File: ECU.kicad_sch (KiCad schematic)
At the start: 62 parts, among them J1 Solenoid 0, J10 Thermocouple 3, J2 Solenoid 1, J3 Solenoid 2, J4 Solenoid 3, J5 Solenoid 4, J6 Solenoid 5, J7 Thermocouple 0, J8 Thermocouple 1, J9 Thermocouple 2, U1 Teensy4.1, U10 MAX31855, U11 MAX31855, U2 OPA357, U3 OPA357, U4 OPA357, U5 OPA357, U6 OPA357, U7 OPA357, U8 MAX31855, U9 MAX31855

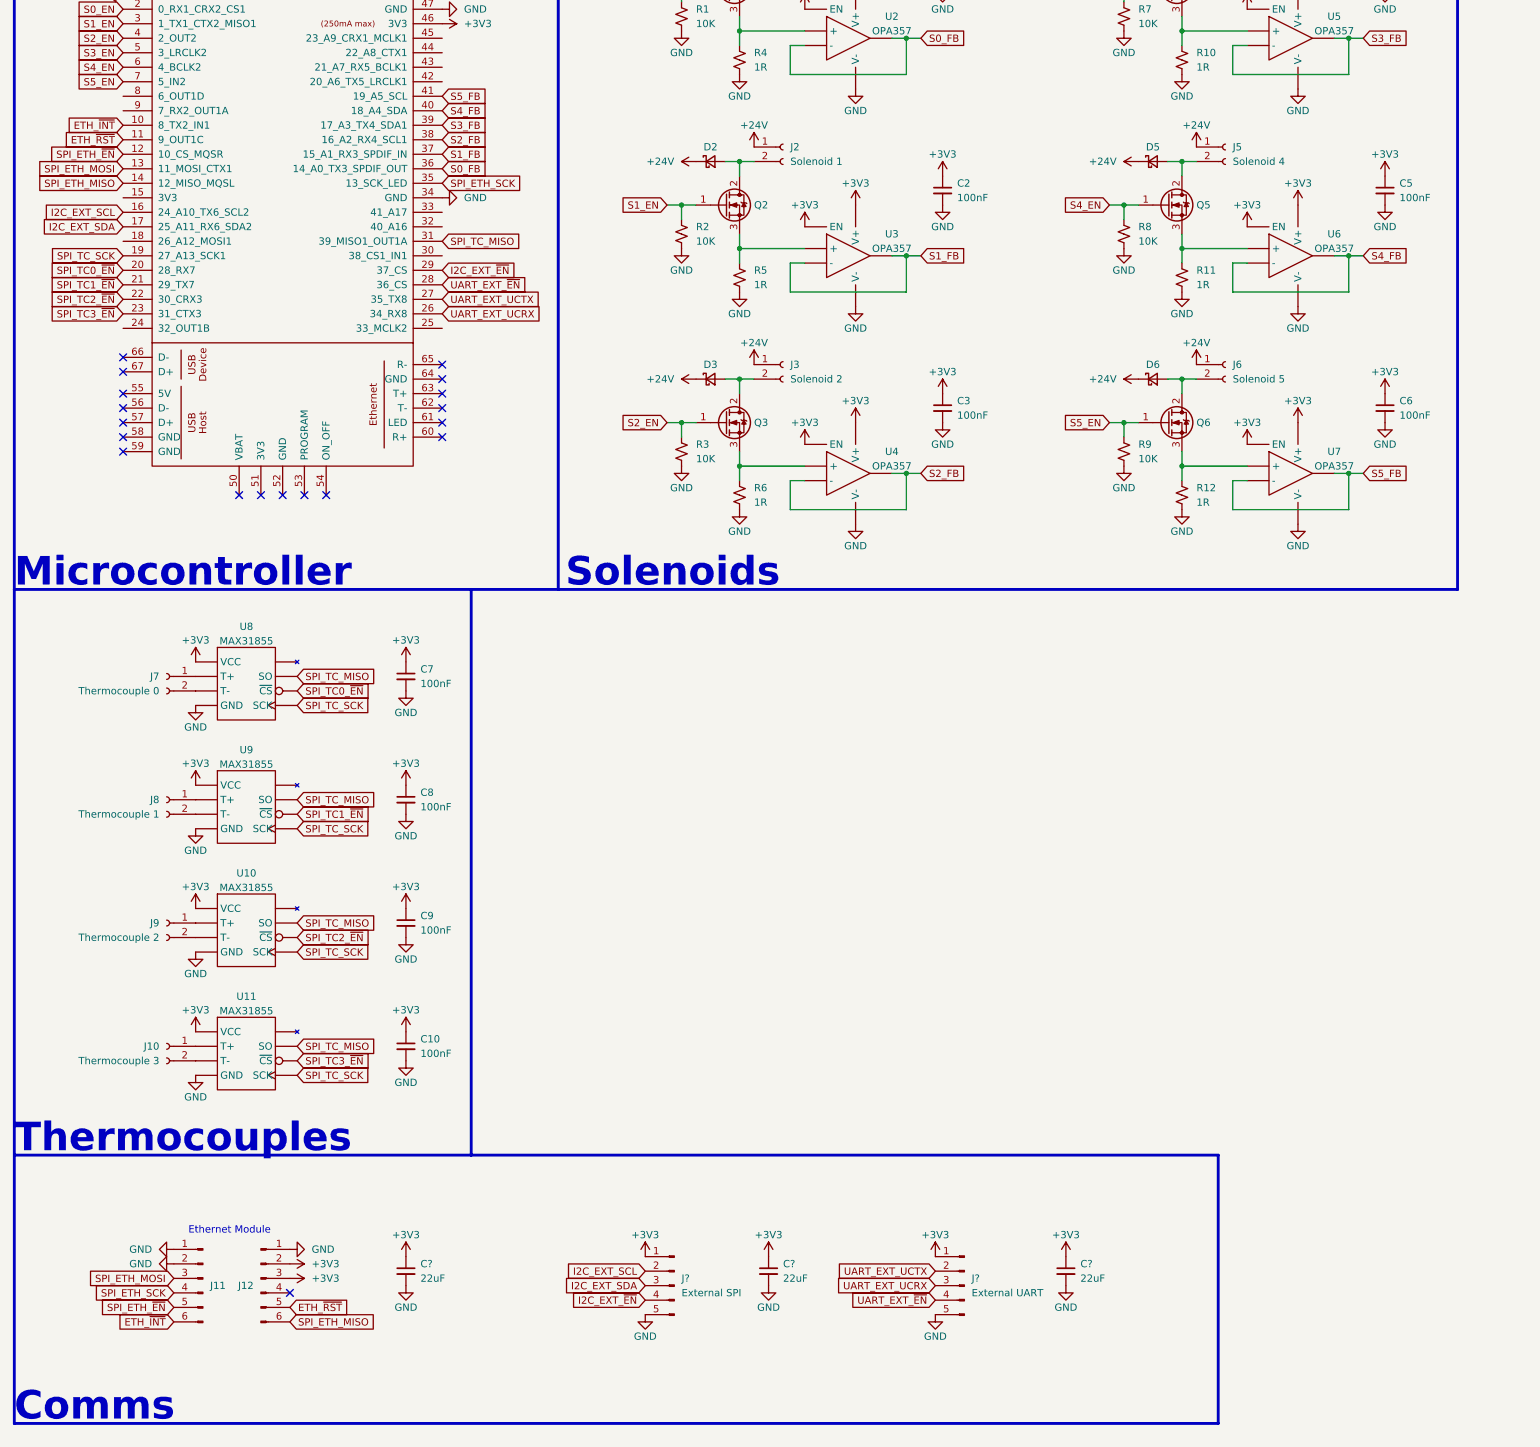
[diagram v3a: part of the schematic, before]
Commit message: Reuse ethernet SPI bus for external devices
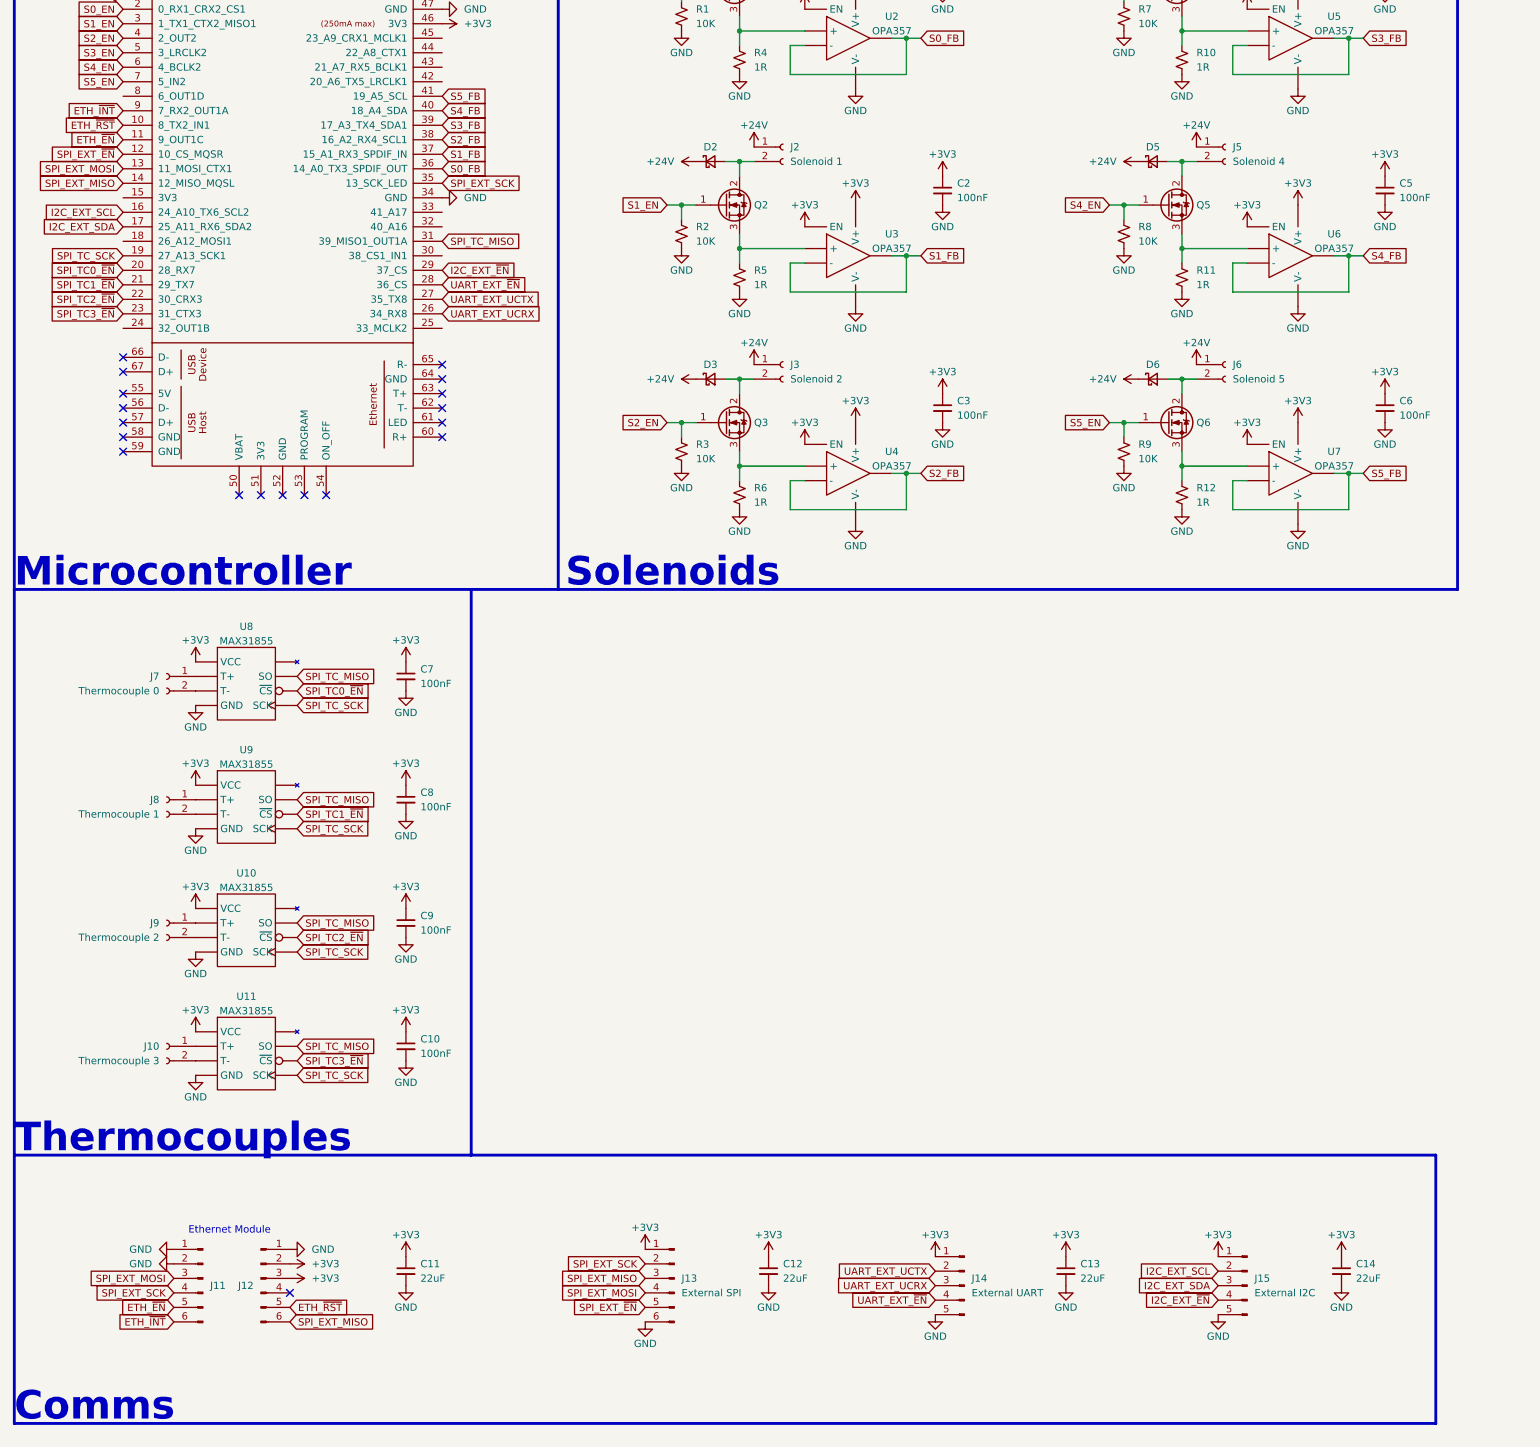
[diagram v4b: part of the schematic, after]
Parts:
- removed J?: External SPI, Connector_PinHeader_2.54mm:PinHeader_1x05_P2.54mm_Vertical, symbol Connector:Conn_01x05_Male
- added C14: 22uF, Capacitor_SMD:C_0805_2012Metric, symbol Device:C_Small
- added J13: External SPI, Connector_PinHeader_2.54mm:PinHeader_1x06_P2.54mm_Vertical, symbol Connector:Conn_01x06_Male
- added J15: External I2C, Connector_PinHeader_2.54mm:PinHeader_1x05_P2.54mm_Vertical, symbol Connector:Conn_01x05_Male
- gave numbers to parts that had none: 4
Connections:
- net +3V3: now also C14.1, J13.1 (Pin_1), J15.1 (Pin_1)
- net ETH_~{INT}: now also U1.9 (7_RX2_OUT1A); no longer U1.10 (8_TX2_IN1)
- net ETH_~{RST}: now also U1.10 (8_TX2_IN1); no longer U1.11 (9_OUT1C)
- net GND: now also C14.2, J13.6 (Pin_6), J15.5 (Pin_5)
- net I2C_EXT_SCL: now also J15.2 (Pin_2)
- net I2C_EXT_SDA: now also J15.3 (Pin_3)
- net I2C_EXT_~{EN}: now also J15.4 (Pin_4)
- net SPI_ETH_MISO renamed SPI_EXT_MISO
- net SPI_EXT_MISO: now also J13.3 (Pin_3)
- net SPI_ETH_MOSI renamed SPI_EXT_MOSI
- net SPI_EXT_MOSI: now also J13.4 (Pin_4)
- net SPI_ETH_SCK renamed SPI_EXT_SCK
- net SPI_EXT_SCK: now also J13.2 (Pin_2)
- net SPI_ETH_~{EN} renamed ETH_~{EN}
- net ETH_~{EN}: now also U1.11 (9_OUT1C); no longer U1.12 (10_CS_MQSR)
- new net SPI_EXT_~{EN}: J13.5 (Pin_5), U1.12 (10_CS_MQSR)

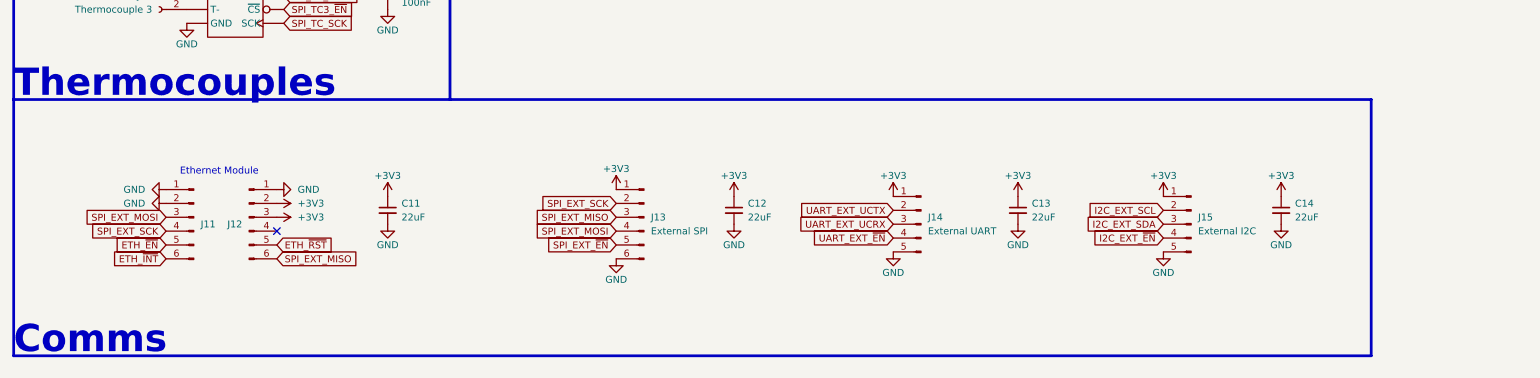
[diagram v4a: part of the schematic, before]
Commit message: Add I2C bus pullups
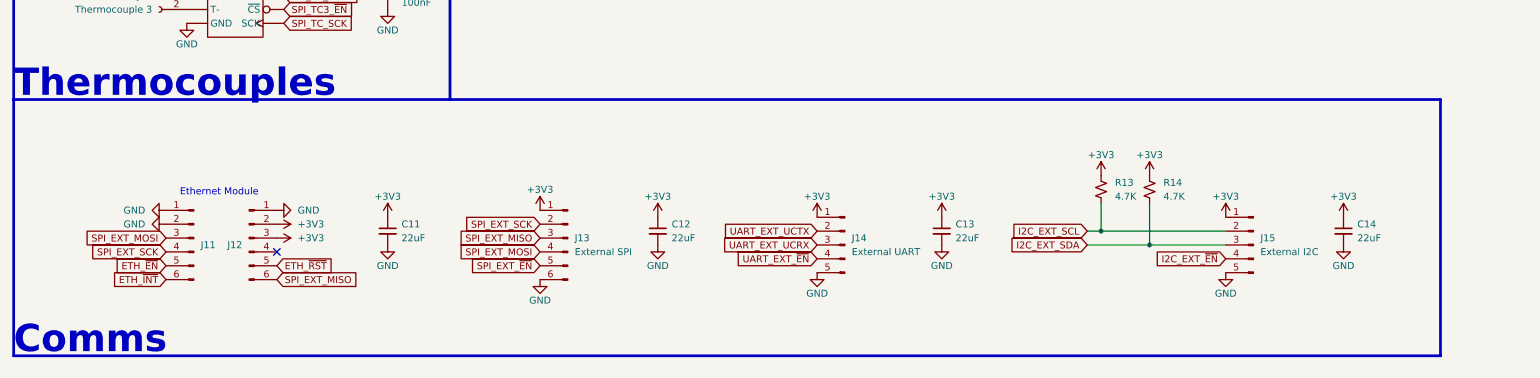
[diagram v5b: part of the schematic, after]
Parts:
- added R13, R14: 4.7K, Resistor_SMD:R_0603_1608Metric, symbol Device:R_Small_US
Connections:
- net +3V3: now also R13.1, R14.1
- net I2C_EXT_SCL: now also R13.2
- net I2C_EXT_SDA: now also R14.2
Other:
- moved on the sheet: C11, C12, C13, C14, J11, J12, J13, J14, J15

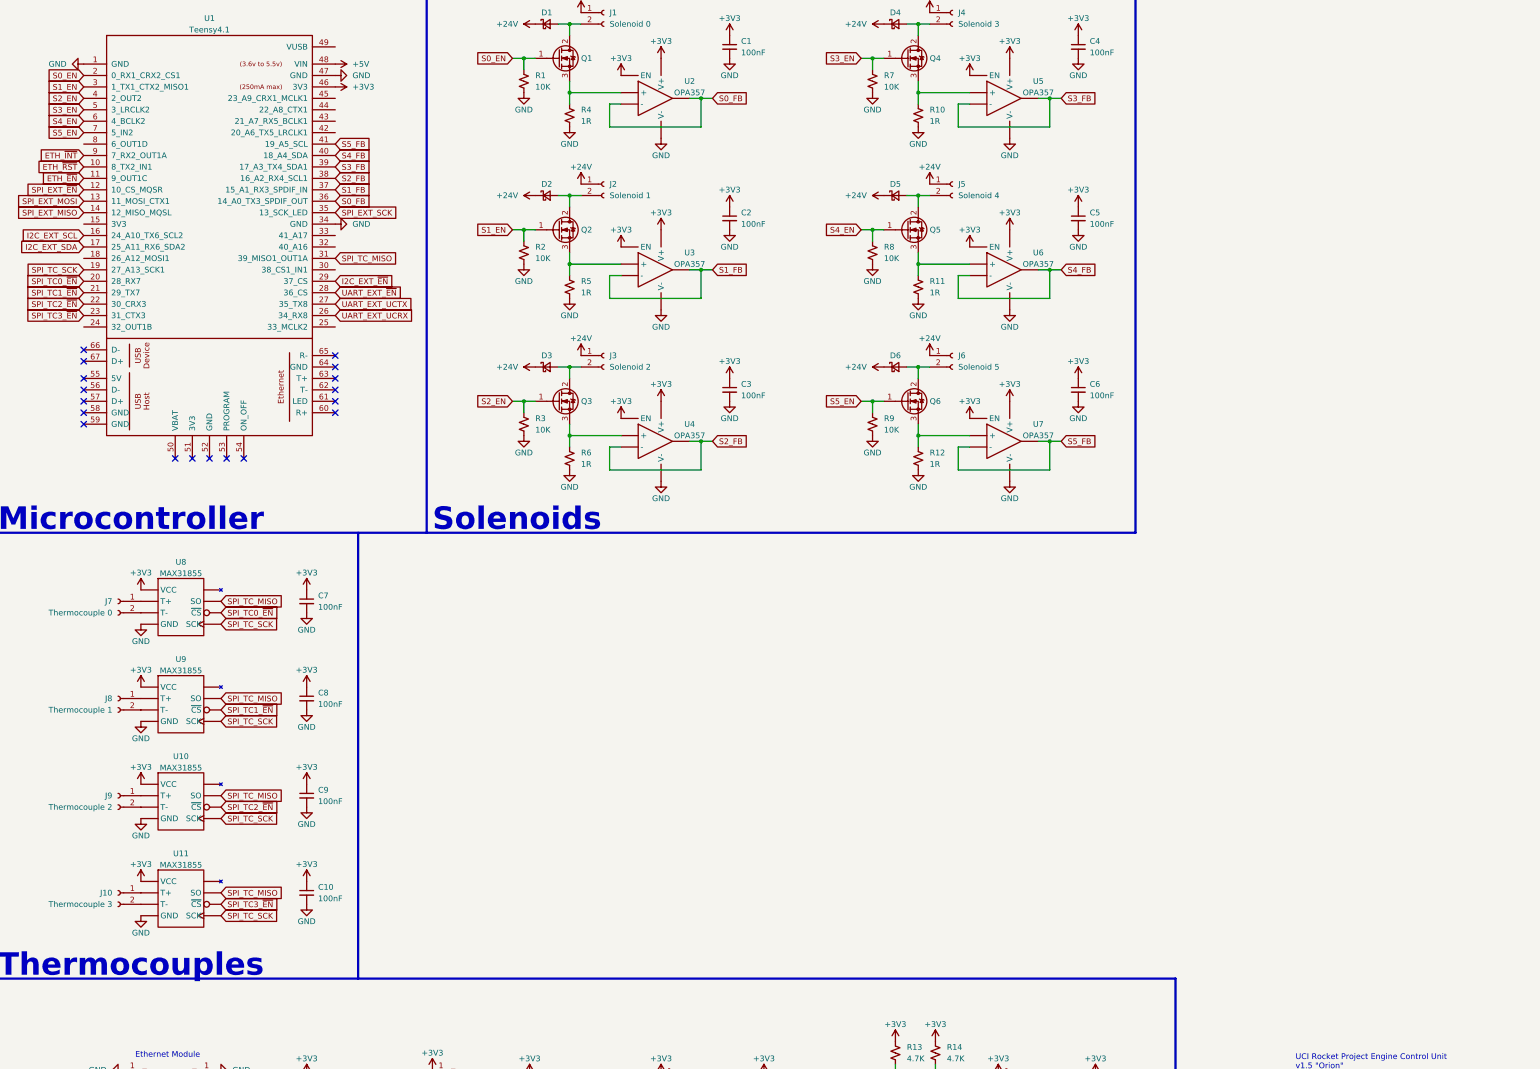
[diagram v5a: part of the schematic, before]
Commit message: Add pressure transducer design
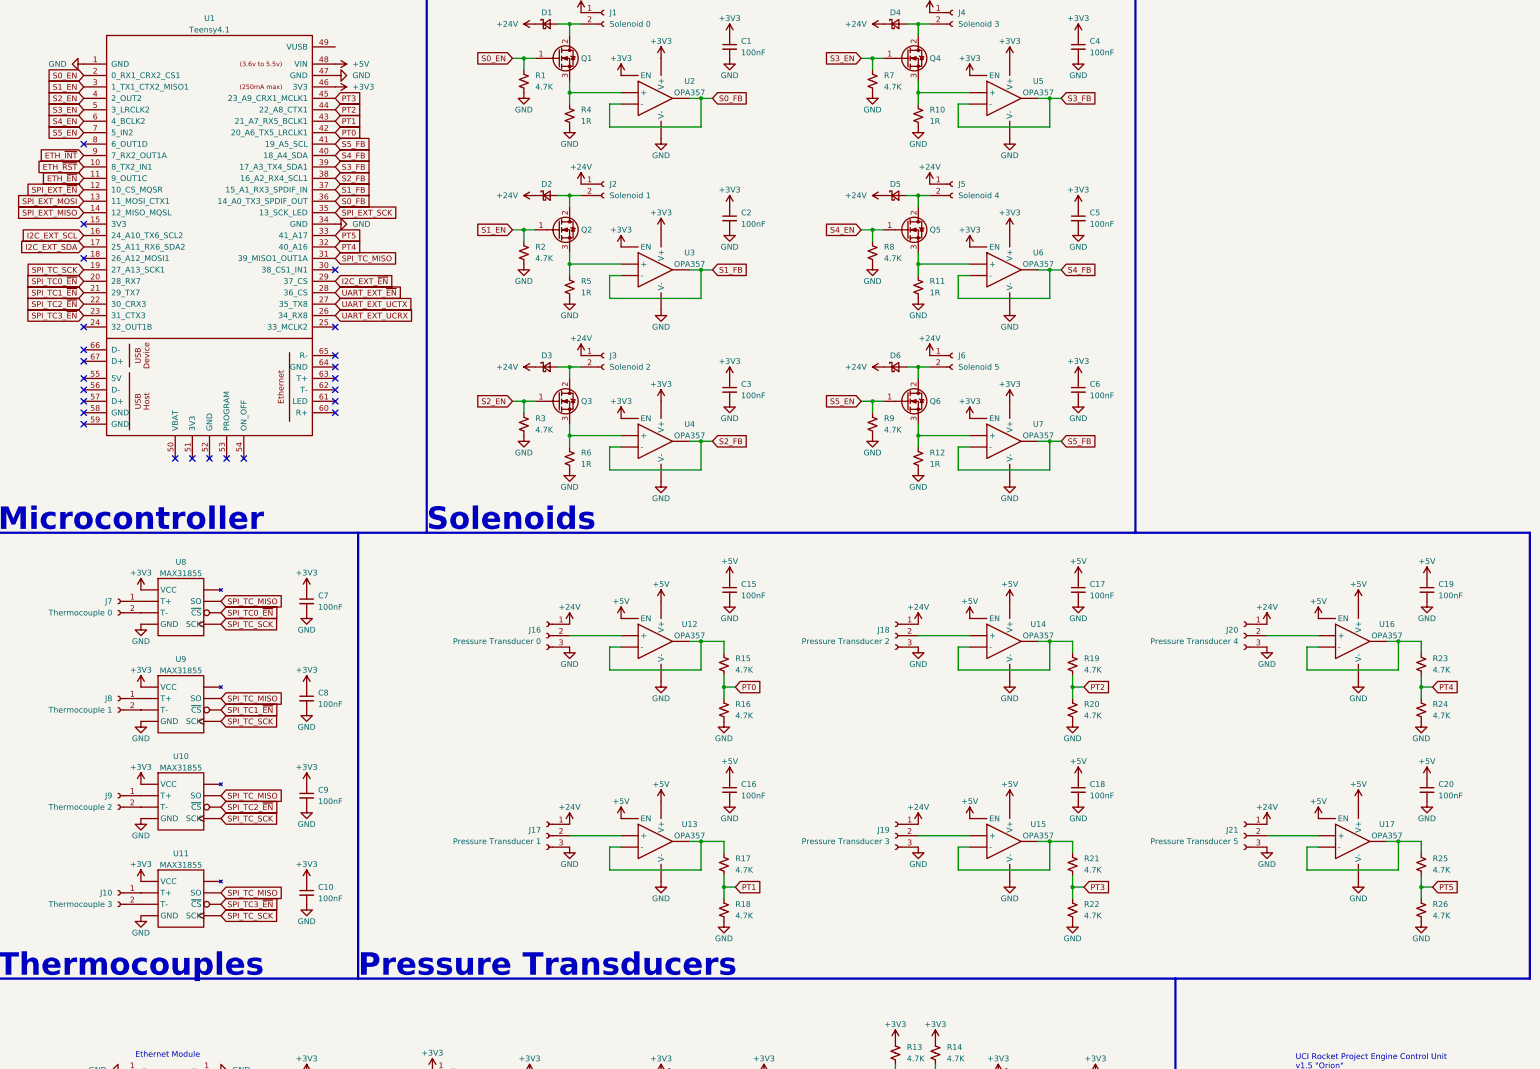
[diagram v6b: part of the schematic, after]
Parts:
- added C15, C16, C17, C18, C19, C20: 100nF, Capacitor_SMD:C_0603_1608Metric, symbol Device:C_Small
- added J16: Pressure Transducer 0, TerminalBlock:TerminalBlock_bornier-3_P5.08mm, symbol Connector:Conn_01x03_Female
- added J17: Pressure Transducer 1, TerminalBlock:TerminalBlock_bornier-3_P5.08mm, symbol Connector:Conn_01x03_Female
- added J18: Pressure Transducer 2, TerminalBlock:TerminalBlock_bornier-3_P5.08mm, symbol Connector:Conn_01x03_Female
- added J19: Pressure Transducer 3, TerminalBlock:TerminalBlock_bornier-3_P5.08mm, symbol Connector:Conn_01x03_Female
- added J20: Pressure Transducer 4, TerminalBlock:TerminalBlock_bornier-3_P5.08mm, symbol Connector:Conn_01x03_Female
- added J21: Pressure Transducer 5, TerminalBlock:TerminalBlock_bornier-3_P5.08mm, symbol Connector:Conn_01x03_Female
- added R15, R16, R17, R18, R19, R20, R21, R22, R23, R24, R25, R26: 4.7K, Resistor_SMD:R_0603_1608Metric, symbol Device:R_Small_US
- added U12, U13, U14, U15, U16, U17: OPA357, Package_TO_SOT_SMD:SOT-23-6, symbol ECU:OPA357
- J14, J15: Part # Generic 6x2.54 Pin Header -> Generic 5x2.54 Pin Header
- R1, R2, R3, R7, R8, R9: value 10K -> 4.7K; Part # Generic 10K 0603 Resistor -> Generic 4.7K 0603 Resistor
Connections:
- net +24V: now also J16.1 (Pin_1), J17.1 (Pin_1), J18.1 (Pin_1), J19.1 (Pin_1), J20.1 (Pin_1), J21.1 (Pin_1)
- net +5V: now also C15.1, C16.1, C17.1, C18.1, C19.1, C20.1, U12.5 (EN), U12.6 (V+), U13.5 (EN), U13.6 (V+), U14.5 (EN), U14.6 (V+), U15.5 (EN), U15.6 (V+), U16.5 (EN), U16.6 (V+), U17.5 (EN), U17.6 (V+)
- net GND: now also C15.2, C16.2, C17.2, C18.2, C19.2, C20.2, J16.3 (Pin_3), J17.3 (Pin_3), J18.3 (Pin_3), J19.3 (Pin_3), J20.3 (Pin_3), J21.3 (Pin_3), R16.2, R18.2, R20.2, R22.2, R24.2, R26.2, U12.2 (V-), U13.2 (V-), U14.2 (V-), U15.2 (V-), U16.2 (V-), U17.2 (V-)
- net PT4: now reaches U1.32 (40_A16)
- net PT4: now also R23.2, R24.1
- net PT5: now reaches U1.33 (41_A17)
- net PT5: now also R25.2, R26.1
- net PT0: now reaches U1.42 (20_A6_TX5_LRCLK1)
- net PT0: now also R15.2, R16.1
- net PT1: now reaches U1.43 (21_A7_RX5_BCLK1)
- net PT1: now also R17.2, R18.1
- net PT2: now reaches U1.44 (22_A8_CTX1)
- net PT2: now also R19.2, R20.1
- net PT3: now reaches U1.45 (23_A9_CRX1_MCLK1)
- net PT3: now also R21.2, R22.1
- new net: J16.2 (Pin_2), U12.3 (+)
- new net: R19.1, U14.1, U14.4 (-)
- new net: J18.2 (Pin_2), U14.3 (+)
- new net: R25.1, U17.1, U17.4 (-)
- new net: J21.2 (Pin_2), U17.3 (+)
- new net: R17.1, U13.1, U13.4 (-)
- new net: J17.2 (Pin_2), U13.3 (+)
- new net: R15.1, U12.1, U12.4 (-)
- new net: R23.1, U16.1, U16.4 (-)
- new net: J20.2 (Pin_2), U16.3 (+)
- new net: R21.1, U15.1, U15.4 (-)
- new net: J19.2 (Pin_2), U15.3 (+)
- no-connect marks 19 -> 25
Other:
- note added: "Pressure Transducers"
